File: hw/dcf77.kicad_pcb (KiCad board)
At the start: 2 copper layers, 23 parts, among them J1 AVR-ISP-6, J2 FTDI, J3 DHT22_Sensor, J4 DCF77_Decoder, SW1 MODE, SW2 SET, SW3 ADJ, U1 ATmega328P-PU, U2 DE122-XX-XX, U3 74HC595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

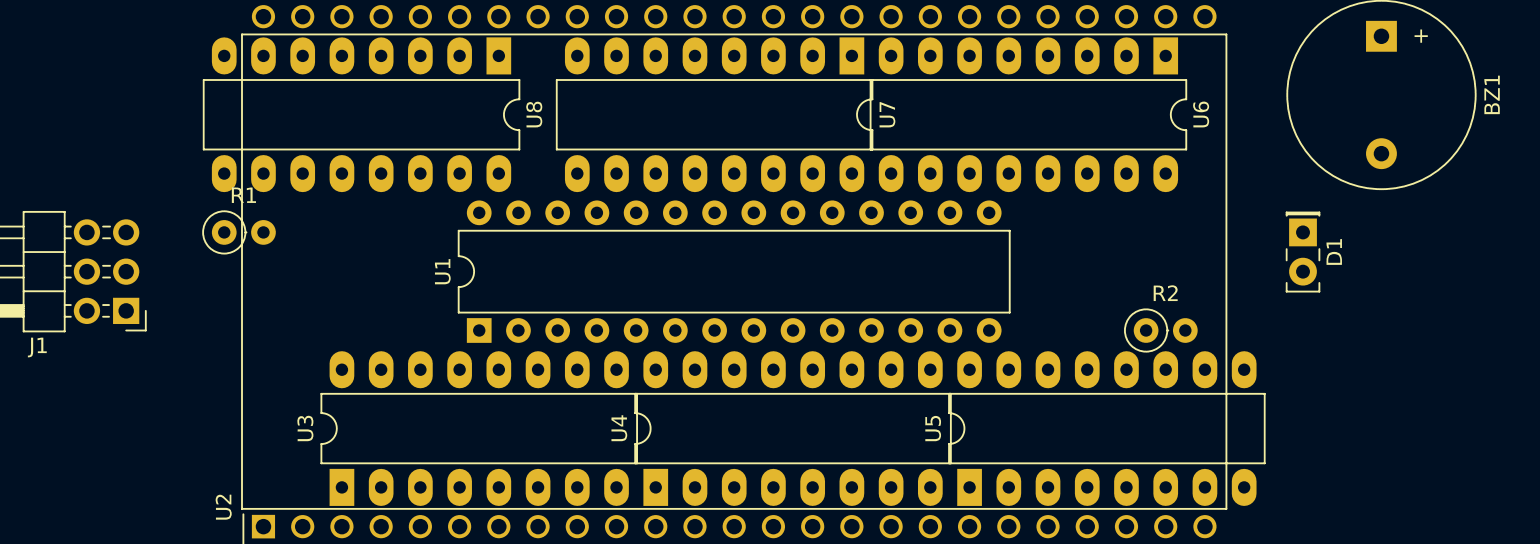
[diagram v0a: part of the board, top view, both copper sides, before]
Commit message: Add PCB footprint for LCD backlight
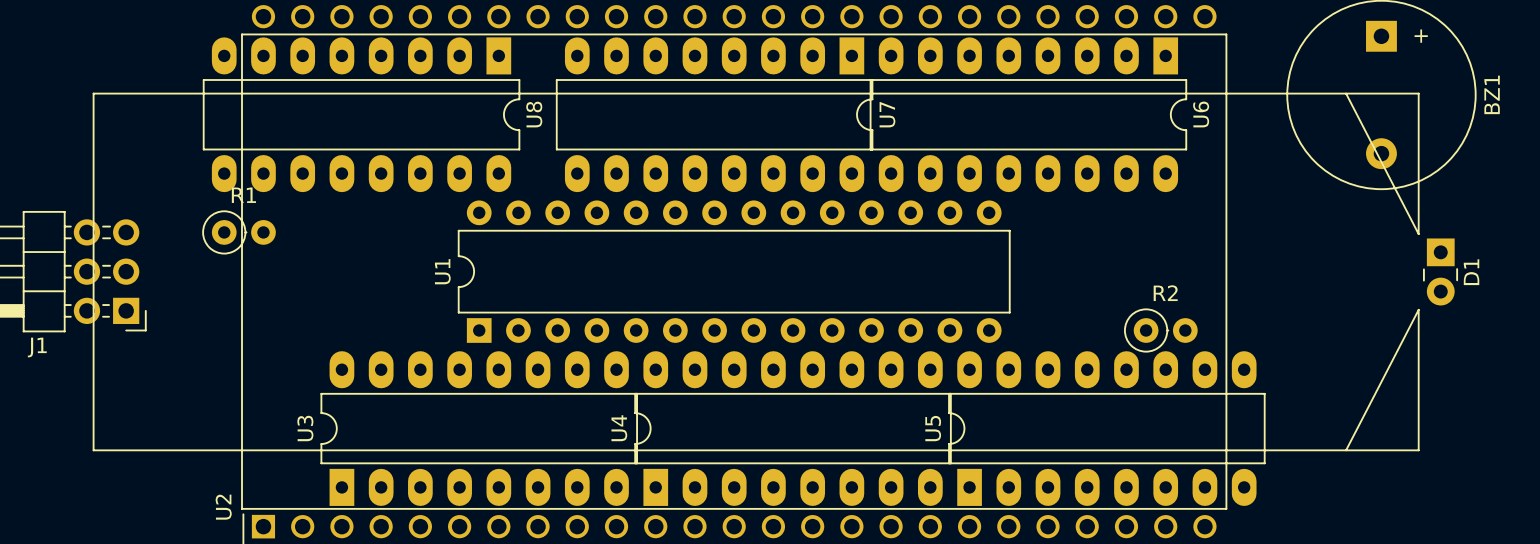
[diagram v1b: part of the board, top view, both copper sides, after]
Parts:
- D1: footprint LED_THT:LED_Rectangular_W5.0mm_H2.0mm -> tomscii:LED_backlight_COM0621
- moved D1 8.98 mm to (109.2, 59.7), turned to 0 degrees
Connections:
- R1 pad 1: /RST- -> VCC
- R1 pad 2: Net-(R1-Pad2) -> /RST-
- U1 pad 1: Net-(R1-Pad2) -> /RST-
